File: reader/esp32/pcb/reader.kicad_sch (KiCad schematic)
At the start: 28 parts, among them J1 Conn_01x06, J2 Conn_01x02, J3 Conn_01x04, J4 Conn_01x02, Q1 MMBT3904, Q2 MMBT3904, U1 ESP32-WROOM-32U, U2 RF125-PS, U3 CH340C, U4 74LVC1T45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

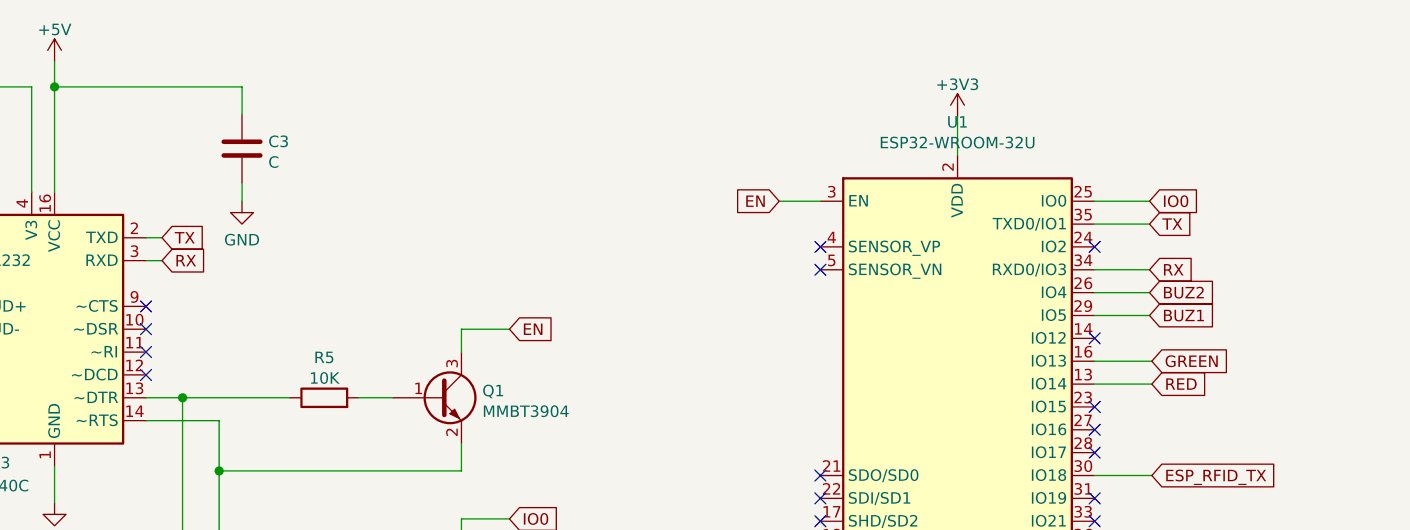
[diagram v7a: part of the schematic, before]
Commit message: Fix switched RX/TX, adjust dimensions.
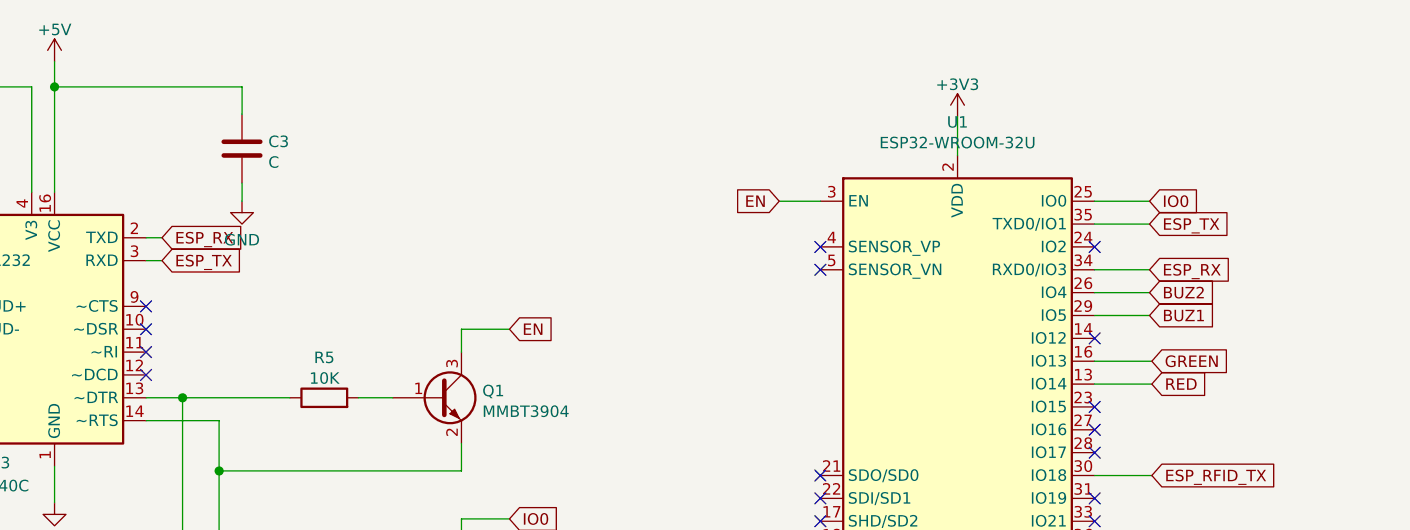
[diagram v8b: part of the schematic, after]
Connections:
- net RX renamed ESP_RX
- net ESP_RX: now also U3.2 (TXD); no longer U3.3 (RXD)
- net TX renamed ESP_TX
- net ESP_TX: now also U3.3 (RXD); no longer U3.2 (TXD)
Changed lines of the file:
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@@
     (stroke (width 0) (type solid) (color 0 0 0 0))
   )
-  (global_label "TX" (shape input) (at 67.818 55.88 0) (fields_autoplaced)
+  (global_label "ESP_RX" (shape input) (at 67.818 55.88 0) (fields_autoplaced)
     (effects (font (size 1.27 1.27)) (justify left))
-    (property "Intersheet References" "${INTERSHEET_REFS}" (id 0) (at 72.4082 55.8006 0)
+    (property "Intersheet References" "${INTERSHEET_REFS}" (id 0) (at 77.3068 55.8006 0)
       (effects (font (size 1.27 1.27)) (justify left) hide)
     )
   )
-  (global_label "RX" (shape input) (at 67.818 58.42 0) (fields_autoplaced)
+  (global_label "ESP_TX" (shape input) (at 67.818 58.42 0) (fields_autoplaced)
     (effects (font (size 1.27 1.27)) (justify left))
-    (property "Intersheet References" "${INTERSHEET_REFS}" (id 0) (at 72.7106 58.3406 0)
+    (property "Intersheet References" "${INTERSHEET_REFS}" (id 0) (at 77.0044 58.3406 0)
       (effects (font (size 1.27 1.27)) (justify left) hide)
     )
@@
     )
   )
-  (global_label "TX" (shape input) (at 177.546 54.356 0) (fields_autoplaced)
+  (global_label "ESP_TX" (shape input) (at 177.546 54.356 0) (fields_autoplaced)
     (effects (font (size 1.27 1.27)) (justify left))
-    (property "Intersheet References" "${INTERSHEET_REFS}" (id 0) (at 182.1362 54.2766 0)
+    (property "Intersheet References" "${INTERSHEET_REFS}" (id 0) (at 186.7324 54.2766 0)
       (effects (font (size 1.27 1.27)) (justify left) hide)
     )
   )
-  (global_label "RX" (shape input) (at 177.546 59.436 0) (fields_autoplaced)
+  (global_label "ESP_RX" (shape input) (at 177.546 59.436 0) (fields_autoplaced)
     (effects (font (size 1.27 1.27)) (justify left))
-    (property "Intersheet References" "${INTERSHEET_REFS}" (id 0) (at 182.4386 59.3566 0)
+    (property "Intersheet References" "${INTERSHEET_REFS}" (id 0) (at 187.0348 59.3566 0)
       (effects (font (size 1.27 1.27)) (justify left) hide)
     )
